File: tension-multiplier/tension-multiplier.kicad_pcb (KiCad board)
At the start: 2 copper layers, 18 x 12 mm, 4 parts, among them J1 Conn_01x03_Pin, J2 Conn_01x02_Pin, J3 Conn_01x02_Pin, U1 AD633ARZ

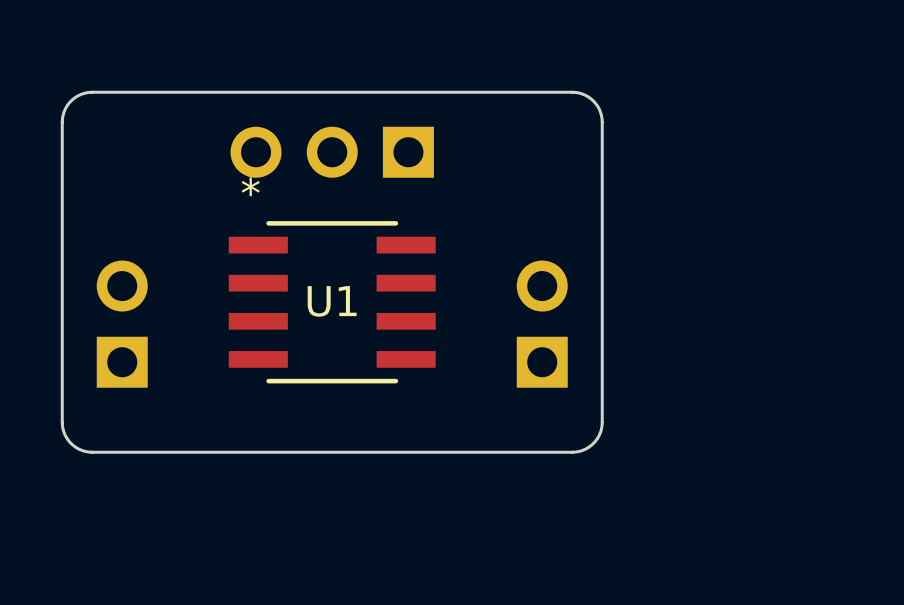
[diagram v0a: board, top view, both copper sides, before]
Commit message: Finishes version 0.1 of Analog Multiplier Module
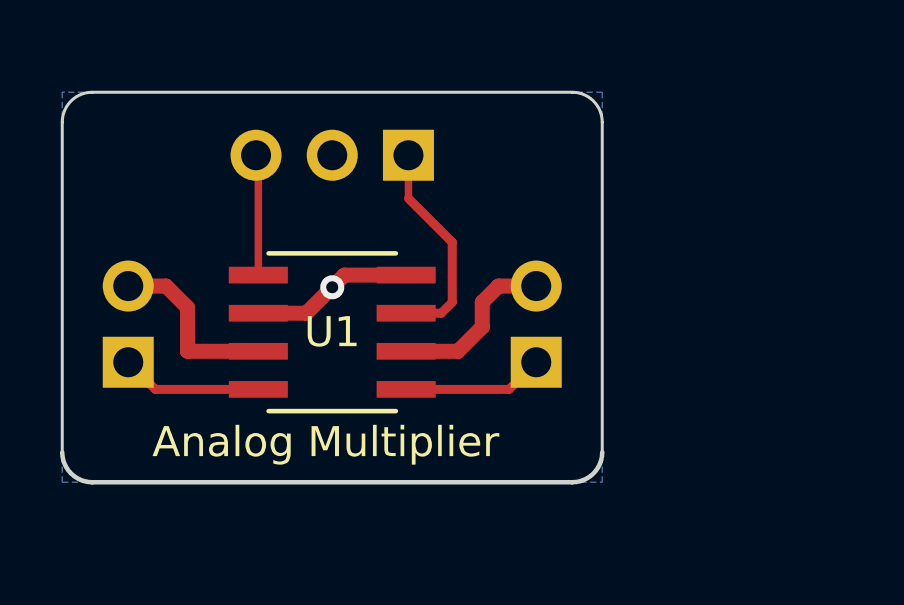
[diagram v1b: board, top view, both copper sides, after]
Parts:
- moved U1 1.00 mm to (144.0, 89.0)
- moved J2 0.20 mm to (150.8, 90.0)
- moved J3 0.20 mm to (137.2, 90.0)
- moved J1 0.10 mm to (146.5, 83.1)
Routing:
- net Net-(J1-Pin_1): track 0.00 -> 7.19 mm
- net VEE: track 0.00 -> 6.09 mm
- net VDD: track 0.00 -> 5.72 mm
- net GND: track 0.71 -> 5.45 mm, vias 0 -> 1
- net Net-(J3-Pin_1): track 0.00 -> 4.71 mm
- net Net-(J2-Pin_1): track 0.00 -> 4.71 mm
- net Net-(J1-Pin_3): track 0.00 -> 4.58 mm
- added copper zone on B.Cu, net GND
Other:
- board size 18 x 12 mm -> 18 x 13 mm
- board text added: "Analog Multiplier"
- board text added: "GND"
- board text added: "Uw"
- board text added: "Ux"
- board text added: "Uy"
- board text added: "Uz"
- board text added: "V+"
- board text added: "V-"
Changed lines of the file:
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@@
   )
   (paper "A4")
+  (title_block
+    (title "Analog Voltage Multiplier Module Board")
+    (date "2024-02-06")
+    (rev "0.1")
+    (company "Carlos Craveiro")
+    (comment 1 "Part of the project Einstein-Boltzmann")
+  )
   (layers
     (0 "F.Cu" signal)
@@
   (net 7 "VEE")
   (footprint "footprints:R_8_ADI" (layer "F.Cu")
-    (at 144 88)
+    (at 144 89)
     (tags "AD633ARZ ")
     (property "Sheetfile" "tension-multiplier.kicad_sch")
@@
     (attr smd)
     (fp_text reference "U1" (at 0 0 unlocked) (layer "F.SilkS")
+        (effects (font (size 1 1) (thickness 0.2)))
+    )
+    (fp_text value "AD633ARZ" (at 0 0 unlocked) (layer "F.Fab")
+        (effects (font (size 1 1) (thickness 0.2)))
+    )
+    (fp_text user "*" (at -2.7178 -3.606 unlocked) (layer "F.SilkS") hide
         (effects (font (size 1 1) (thickness 0.15)))
     )
-    (fp_text value "AD633ARZ" (at 0 0 unlocked) (layer "F.Fab")
+    (fp_text user "*" (at -2.7178 -3.606 unlocked) (layer "F.SilkS") hide
         (effects (font (size 1 1) (thickness 0.15)))
     )
-    (fp_text user "*" (at -2.7178 -3.606 unlocked) (layer "F.SilkS")
-        (effects (font (size 1 1) (thickness 0.15)))
-    )
-    (fp_text user "*" (at -2.7178 -3.606) (layer "F.SilkS")
-        (effects (font (size 1 1) (thickness 0.15)))
+    (fp_text user "${REFERENCE}" (at 0 0 unlocked) (layer "F.Fab")
+        (effects (font (size 1 1) (thickness 0.2) bold))
     )
     (fp_text user "*" (at -1.6129 -2.4257 unlocked) (layer "F.Fab")
         (effects (font (size 1 1) (thickness 0.15)))
     )
-    (fp_text user "${REFERENCE}" (at 0 0 unlocked) (layer "F.Fab")
-        (effects (font (size 1 1) (thickness 0.15)))
-    )
-    (fp_text user "*" (at -1.6129 -2.4257) (layer "F.Fab")
+    (fp_text user "*" (at -1.6129 -2.4257 unlocked) (layer "F.Fab")
         (effects (font (size 1 1) (thickness 0.15)))
     )
@@
   )
   (footprint "Connector_PinHeader_2.54mm:PinHeader_1x03_P2.54mm_Vertical" (layer "B.Cu")
-    (at 146.54 83 90)
+    (at 146.54 83.1 90)
     (descr "Through hole straight pin header, 1x03, 2.54mm pitch, single row")
     (tags "Through hole pin header THT 1x03 2.54mm single row")
@@
     (attr through_hole)
     (fp_text reference "J1" (at 0 2.33 90) (layer "B.SilkS")
-        (effects (font (size 1 1) (thickness 0.15)) (justify mirror))
+        (effects (font (size 1 1) (thickness 0.2) bold) (justify mirror))
     )
     (fp_text value "Conn_01x03_Pin" (at 0 -7.41 90) (layer "B.Fab")
-        (effects (font (size 1 1) (thickness 0.15)) (justify mirror))
+        (effects (font (size 1 1) (thickness 0.2)) (justify mirror))
     )
     (fp_text user "${REFERENCE}" (at 0 -2.54 -360) (layer "B.Fab")
-        (effects (font (size 1 1) (thickness 0.15)) (justify mirror))
+        (effects (font (size 1 1) (thickness 0.2)) (justify mirror))
     )
     (fp_line (start -1.33 -6.41) (end 1.33 -6.41)
@@
   )
   (footprint "Connector_PinHeader_2.54mm:PinHeader_1x02_P2.54mm_Vertical" (layer "B.Cu")
-    (at 137 90)
+    (at 137.2 90)
     (descr "Through hole straight pin header, 1x02, 2.54mm pitch, single row")
     (tags "Through hole pin header THT 1x02 2.54mm single row")
@@
     (property "ki_keywords" "connector")
     (attr through_hole)
-    (fp_text reference "J3" (at 0 2.33) (layer "B.SilkS")
-        (effects (font (size 1 1) (thickness 0.15)) (justify mirror))
+    (fp_text reference "J3" (at 0 2.5 180) (layer "B.SilkS")
+        (effects (font (size 1 1) (thickness 0.2) bold) (justify mirror))
     )
     (fp_text value "Conn_01x02_Pin" (at 0 -4.87) (layer "B.Fab")
-        (effects (font (size 1 1) (thickness 0.15)) (justify mirror))
+        (effects (font (size 1 1) (thickness 0.2)) (justify mirror))
     )
     (fp_text user "${REFERENCE}" (at 0 -1.27 90) (layer "B.Fab")
@@
   )
   (footprint "Connector_PinHeader_2.54mm:PinHeader_1x02_P2.54mm_Vertical" (layer "B.Cu")
-    (at 151 90)
+    (at 150.8 90)
     (descr "Through hole straight pin header, 1x02, 2.54mm pitch, single row")
     (tags "Through hole pin header THT 1x02 2.54mm single row")
@@
     (property "ki_keywords" "connector")
     (attr through_hole)
-    (fp_text reference "J2" (at 0 2.33) (layer "B.SilkS")
-        (effects (font (size 1 1) (thickness 0.15)) (justify mirror))
+    (fp_text reference "J2" (at 0 2.5 180) (layer "B.SilkS")
+        (effects (font (size 1 1) (thickness 0.2) bold) (justify mirror))
     )
     (fp_text value "Conn_01x02_Pin" (at 0 -4.87) (layer "B.Fab")
@@
     )
   )
-  (gr_line (start 135 92) (end 135 82)
+  (gr_line (start 135 93) (end 135 82)
     (stroke (width 0.1) (type default)) (layer "Edge.Cuts"))
-  (gr_arc (start 153 92) (mid 152.707107 92.707107) (end 152 93)
-    (stroke (width 0.1) (type default)) (layer "Edge.Cuts"))
+  (gr_line (start 136 94) (end 152 94)
+    (stroke (width 0.15) (type default)) (layer "Edge.Cuts"))
   (gr_line (start 136 81) (end 152 81)
-    (stroke (width 0.1) (type default)) (layer "Edge.Cuts"))
-  (gr_arc (start 136 93) (mid 135.292893 92.707107) (end 135 92)
     (stroke (width 0.1) (type default)) (layer "Edge.Cuts"))
   (gr_arc (start 135 82) (mid 135.292893 81.292893) (end 136 81)
@@
   (gr_arc (start 152 81) (mid 152.707107 81.292893) (end 153 82)
     (stroke (width 0.1) (type default)) (layer "Edge.Cuts"))
-  (gr_line (start 153 92) (end 153 82)
+  (gr_arc (start 136 94) (mid 135.292894 93.707107) (end 135 93)
+    (stroke (width 0.15) (type default)) (layer "Edge.Cuts"))
+  (gr_arc (start 153 93) (mid 152.707107 93.707106) (end 152 94)
+    (stroke (width 0.15) (type default)) (layer "Edge.Cuts"))
+  (gr_line (start 153 93) (end 153 82)
     (stroke (width 0.1) (type default)) (layer "Edge.Cuts"))
-  (gr_line (start 136 93) (end 152 93)
-    (stroke (width 0.1) (type default)) (layer "Edge.Cuts"))
-  (segment (start 141.5362 87.365) (end 142.242199 87.365) (width 0.5) (layer "F.Cu") (net 6))
+  (gr_text "Ux" (at 148 86) (layer "B.SilkS")
+    (effects (font (size 1 1) (thickness 0.2)) (justify left bottom mirror))
+  )
+  (gr_text "Uz" (at 141 90.5) (layer "B.SilkS")
+    (effects (font (size 1 1) (thickness 0.2) bold) (justify left bottom mirror))
+  )
+  (gr_text "V-" (at 141 88) (layer "B.SilkS")
+    (effects (font (size 1 1) (thickness 0.2)) (justify left bottom mirror))
+  )
+  (gr_text "Uw" (at 149 90.5) (layer "B.SilkS")
+    (effects (font (size 1 1) (thickness 0.2) bold) (justify left bottom mirror))
+  )
+  (gr_text "V+" (at 149 88) (layer "B.SilkS")
+    (effects (font (size 1 1) (thickness 0.2) bold) (justify left bottom mirror))
+  )
+  (gr_text "Uy" (at 141.5 86) (layer "B.SilkS")
+    (effects (font (size 1 1) (thickness 0.2) bold) (justify left bottom mirror))
+  )
+  (gr_text "GND" (at 145.5 86) (layer "B.SilkS")
+    (effects (font (size 1 1) (thickness 0.2) bold) (justify left bottom mirror))
+  )
+  (gr_text "Analog Multiplier" (at 138 93.25) (layer "F.SilkS")
+    (effects (font (size 1 1) (thickness 0.2)) (justify left bottom))
+  )
+  (segment (start 148 86) (end 148 88) (width 0.3) (layer "F.Cu") (net 1))
+  (segment (start 146.54 84.54) (end 146.54 83.1) (width 0.25) (layer "F.Cu") (net 1))
+  (segment (start 146.54 84.54) (end 148 86) (width 0.3) (layer "F.Cu") (net 1))
+  (segment (start 147.635 88.365) (end 146.4638 88.365) (width 0.3) (layer "F.Cu") (net 1))
+  (segment (start 148 88) (end 147.635 88.365) (width 0.3) (layer "F.Cu") (net 1))
+  (segment (start 141.5362 87.095) (end 141.5362 83.1762) (width 0.25) (layer "F.Cu") (net 2))
+  (segment (start 141.5362 83.1762) (end 141.46 83.1) (width 0.25) (layer "F.Cu") (net 2))
+  (segment (start 141.5362 83.0762) (end 141.46 83) (width 0.3) (layer "F.Cu") (net 2))
+  (segment (start 141.5362 87.095) (end 141.095 87.095) (width 0.5) (layer "F.Cu") (net 2))
+  (segment (start 150.8 90) (end 149.895 90.905) (width 0.3) (layer "F.Cu") (net 3))
+  (segment (start 149.895 90.905) (end 146.4638 90.905) (width 0.3) (layer "F.Cu") (net 3))
+  (segment (start 138.105 90.905) (end 141.5362 90.905) (width 0.3) (layer "F.Cu") (net 4))
+  (segment (start 137.2 90) (end 138.105 90.905) (width 0.3) (layer "F.Cu") (net 4))
+  (segment (start 149 88.825) (end 148.19 89.635) (width 0.5) (layer "F.Cu") (net 5))
+  (segment (start 148.19 89.635) (end 146.4638 89.635) (width 0.5) (layer "F.Cu") (net 5))
+  (segment (start 149 88) (end 149 88.825) (width 0.5) (layer "F.Cu") (net 5))
+  (segment (start 150.8 87.46) (end 149.54 87.46) (width 0.5) (layer "F.Cu") (net 5))
+  (segment (start 149.54 87.46) (end 149 88) (width 0.5) (layer "F.Cu") (net 5))
+  (segment (start 143.135 88.365) (end 144.405 87.095) (width 0.5) (layer "F.Cu") (net 6))
+  (segment (start 141.5362 88.365) (end 143.135 88.365) (width 0.5) (layer "F.Cu") (net 6))
+  (segment (start 144.405 87.095) (end 146.4638 87.095) (width 0.5) (layer "F.Cu") (net 6))
+  (via (at 144 87.5) (size 0.8) (drill 0.4) (layers "F.Cu" "B.Cu") (net 6))
+  (segment (start 141.5362 89.635) (end 139.175 89.635) (width 0.5) (layer "F.Cu") (net 7))
+  (segment (start 138.46 87.46) (end 137.2 87.46) (width 0.5) (layer "F.Cu") (net 7))
+  (segment (start 139.175 89.635) (end 139.175 88.175) (width 0.5) (layer "F.Cu") (net 7))
+  (segment (start 139.175 88.175) (end 138.46 87.46) (width 0.5) (layer "F.Cu") (net 7))
+  (zone (net 6) (net_name "GND") (layer "B.Cu") (hatch edge 0.5)
+    (connect_pads (clearance 0.3))
+    (min_thickness 0.25) (filled_areas_thickness no)
+    (fill yes (thermal_gap 0.5) (thermal_bridge_width 0.5))
+    (polygon
+      (pts
+        (xy 135 81)
+        (xy 135 94)
+        (xy 153 94)
+        (xy 153 81)
+      )
+    )
+  )
 )
